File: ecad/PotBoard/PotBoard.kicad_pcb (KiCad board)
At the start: 2 copper layers, 35 x 72.8 mm, 38 parts, among them J1 toIOBoard, Q1 2N4401BU, Q2 2N4401BU, U1 RC4558

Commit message: Big commit
Spice Simulations
Finalize ECAD schematic
old MCAD stuff
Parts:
- removed C1: 100u, Capacitor_SMD:C_0805_2012Metric_Pad1.18x1.45mm_HandSolder
- removed C10: CP, Capacitor_SMD:C_0805_2012Metric_Pad1.18x1.45mm_HandSolder
- removed C11: 51p, Capacitor_SMD:C_0805_2012Metric_Pad1.18x1.45mm_HandSolder
- removed C2: 10n, Capacitor_SMD:C_0805_2012Metric_Pad1.18x1.45mm_HandSolder
- removed C3: 47u, Capacitor_SMD:C_0805_2012Metric_Pad1.18x1.45mm_HandSolder
- removed C4: 20n, Capacitor_SMD:C_0805_2012Metric_Pad1.18x1.45mm_HandSolder
- removed C5, C8: 1u, Capacitor_SMD:C_0805_2012Metric_Pad1.18x1.45mm_HandSolder
- removed C6: 0u22, Capacitor_SMD:C_0805_2012Metric_Pad1.18x1.45mm_HandSolder
- removed C7: 220n, Capacitor_SMD:C_0805_2012Metric_Pad1.18x1.45mm_HandSolder
- removed C9: 0u1, Capacitor_SMD:C_0805_2012Metric_Pad1.18x1.45mm_HandSolder
- removed D1, D2, D3: 1N914, Diode_THT:D_DO-35_SOD27_P7.62mm_Horizontal
- removed Q1, Q2: 2N4401BU, digikey-footprints:TO-92-3
- removed R1, R10, R15, R17, R2, R6, R7: 10k, Resistor_SMD:R_0805_2012Metric_Pad1.20x1.40mm_HandSolder
- removed R11: 220, Resistor_SMD:R_0805_2012Metric_Pad1.20x1.40mm_HandSolder
- removed R12, R13, R4, R9: 1k, Resistor_SMD:R_0805_2012Metric_Pad1.20x1.40mm_HandSolder
- removed R14, R5: 501k, Resistor_SMD:R_0805_2012Metric_Pad1.20x1.40mm_HandSolder
- removed R16: 100, Resistor_SMD:R_0805_2012Metric_Pad1.20x1.40mm_HandSolder
- removed R3: 1M5, Resistor_SMD:R_0805_2012Metric_Pad1.20x1.40mm_HandSolder
- removed R8: 51k, Resistor_SMD:R_0805_2012Metric_Pad1.20x1.40mm_HandSolder
- removed U1: RC4558, Package_SO:Texas_R-PDSO-G8_EP2.95x4.9mm_Mask2.4x3.1mm
- added J2: TonePot, Connector_PinSocket_2.00mm:PinSocket_1x03_P2.00mm_Vertical, B.Cu at (102.5, 79.8)
- added J3: VolumePot, Connector_PinSocket_2.00mm:PinSocket_1x03_P2.00mm_Vertical, B.Cu at (93.3, 83.3)
- J1: value toIOBoard -> DrivePot; footprint Connector_PinSocket_1.27mm:PinSocket_2x02_P1.27mm_Vertical -> Connector_PinSocket_2.00mm:PinSocket_1x03_P2.00mm_Vertical
- RV2: value 20k -> 20kb
- moved RV3 49.2 mm to (94.6, 84.6)
- moved RV2 32.2 mm to (102.5, 71.0)
- moved J1 22.2 mm to (111.7, 83.6), turned to 90 degrees
- moved RV1 14.8 mm to (110.4, 84.6)
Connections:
- J1 pad 1: +9V -> Net-(J1-Pad1)
- J1 pad 2: SIG_IN -> Net-(J1-Pad2)
- J1 pad 3: GND -> Net-(J1-Pad3)
- RV1 pad 1: Net-(R8-Pad1) -> Net-(J1-Pad1)
- RV1 pad 2: Net-(C11-Pad1) -> Net-(J1-Pad2)
- RV1 pad 3: Net-(RV1-Pad3) -> Net-(J1-Pad3)
- RV2 pad 1: DRIVE_OUT -> Net-(J2-Pad1)
- RV3 pad 2: VCC -> Net-(J3-Pad2)
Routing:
- net DRIVE_OUT: track 3.96 -> 0.00 mm
- net VCC: track 2.95 -> 0.00 mm
- net Net-(Q2-Pad1): vias 1 -> 0
- net (no net): vias 3 -> 0
- removed copper zone on F.Cu, net +9V
- removed copper zone on B.Cu, net GND
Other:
- board size 35 x 72.8 mm -> 33.5 x 53.3 mm

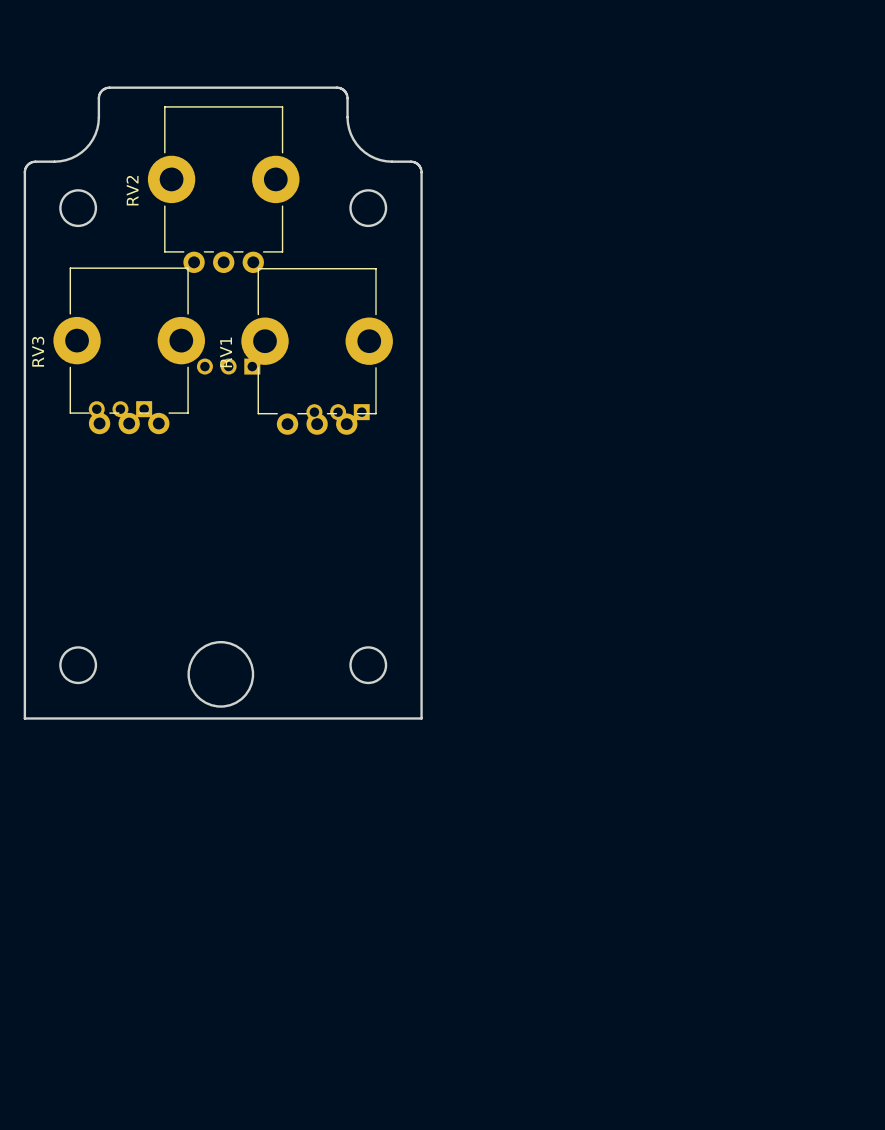
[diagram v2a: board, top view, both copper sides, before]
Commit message: Update layouts with finished mcad
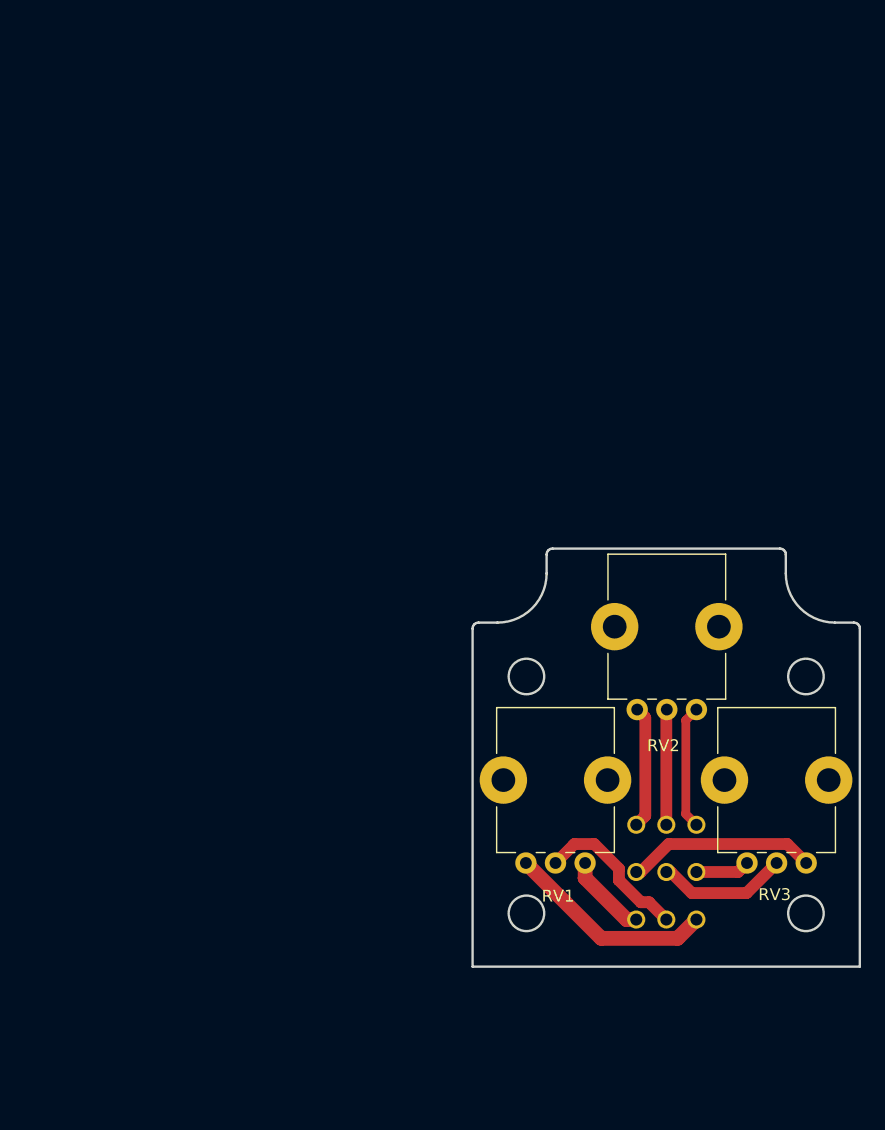
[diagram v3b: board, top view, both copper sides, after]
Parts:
- added G***: LOGO, screaming-panda:Panda_Logo, B.Cu at (137.4, 104.4)
- J1, J2, J3: footprint Connector_PinSocket_2.00mm:PinSocket_1x03_P2.00mm_Vertical -> screaming-panda:C031LFBN-RC
- RV3: value 100ka -> 20ka
- moved RV3 66.1 mm to (149.2, 121.7)
- moved J3 58.9 mm to (137.4, 122.4), turned to 0 degrees
- moved RV2 53.2 mm to (140.0, 108.7)
- moved J2 52.1 mm to (137.4, 118.4), turned to 180 degrees
- moved J1 50.0 mm to (137.4, 126.4), turned to 0 degrees
- moved RV1 42.2 mm to (130.6, 121.7)
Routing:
- net Net-(J1-Pad3): track 0.00 -> 17.7 mm
- net Net-(J3-Pad1): track 0.00 -> 16.0 mm
- net Net-(J1-Pad2): track 0.00 -> 13.2 mm
- net Net-(J3-Pad2): track 0.00 -> 11.1 mm
- net Net-(J2-Pad1): track 0.00 -> 11.1 mm
- net Net-(J2-Pad3): track 0.00 -> 10.3 mm
- net Net-(J2-Pad2): track 0.00 -> 9.74 mm
- net Net-(J1-Pad1): track 0.00 -> 7.04 mm
- net Net-(J3-Pad3): track 0.00 -> 4.59 mm
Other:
- board size 33.5 x 53.3 mm -> 32.7 x 35.3 mm
- board text added: "John McAvoy"
- board text added: "PotBoard"
- board text added: "Screaming Panda 1v0 8/22"

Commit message: Library recovery
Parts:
- removed G***: LOGO, screaming-panda:Panda_Logo

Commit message: Board 1v0
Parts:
- added G***: LOGO, screaming-panda:Panda_Logo, B.Cu at (130.1, 106.2)
- moved RV2 2.63 mm to (137.3, 108.7), turned to 0 degrees
- moved RV3 2.62 mm to (146.6, 121.7), turned to 0 degrees
- moved RV1 2.43 mm to (128.1, 121.6), turned to 0 degrees
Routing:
- net Net-(J1-Pad3): track 17.7 -> 19.1 mm
- net Net-(J3-Pad2): track 11.1 -> 11.8 mm
- net Net-(J2-Pad1): track 11.1 -> 10.3 mm
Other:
- board text added: "08/2022"
- board text added: "Screaming Panda 1v0"
- board text removed: "Screaming Panda 1v0 8/22"

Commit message: Update libraries to j-mcavoy kicad library
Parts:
- removed G***: LOGO, screaming-panda:Panda_Logo
- J1, J2, J3: footprint screaming-panda:C031LFBN-RC -> j-mcavoy:C031LFBN-RC
- RV1, RV2, RV3: footprint screaming-panda:Potentiometer_Bourns_PTV09A-1_Single_Vertical -> j-mcavoy:Potentiometer_Bourns_PTV09A-1_Single_Vertical
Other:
- net class Default removed
